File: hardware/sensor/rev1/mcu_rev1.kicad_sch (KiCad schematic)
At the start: 21 parts, among them IC1 STM8L051F3P6, J1 22-28-4044, J2 M20-9770342

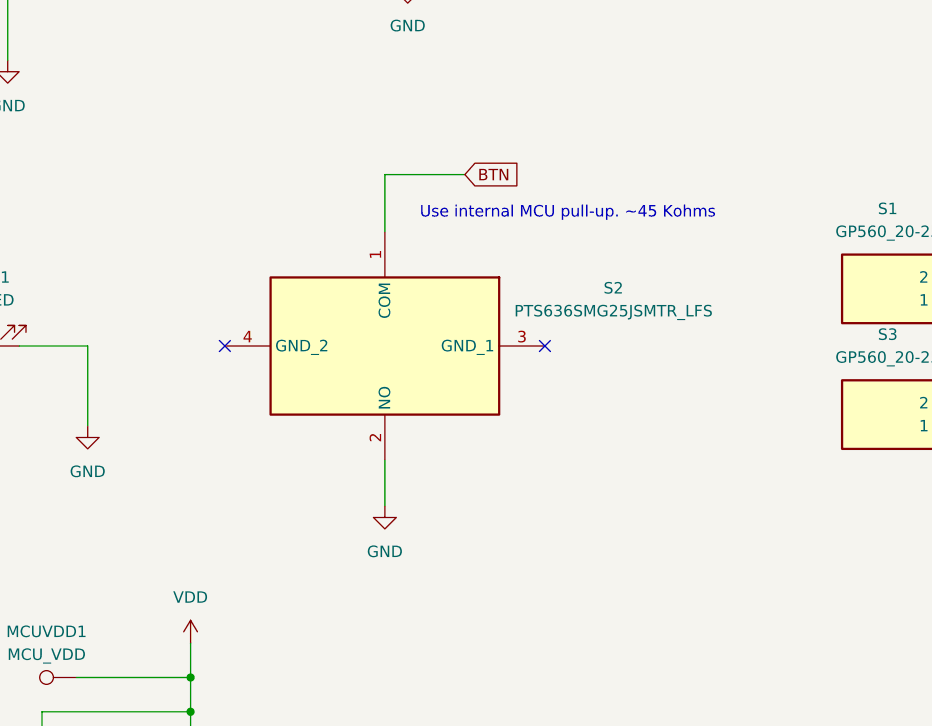
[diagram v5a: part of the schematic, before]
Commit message: EG-70 Adaptions according with JLCPCB production constraints.
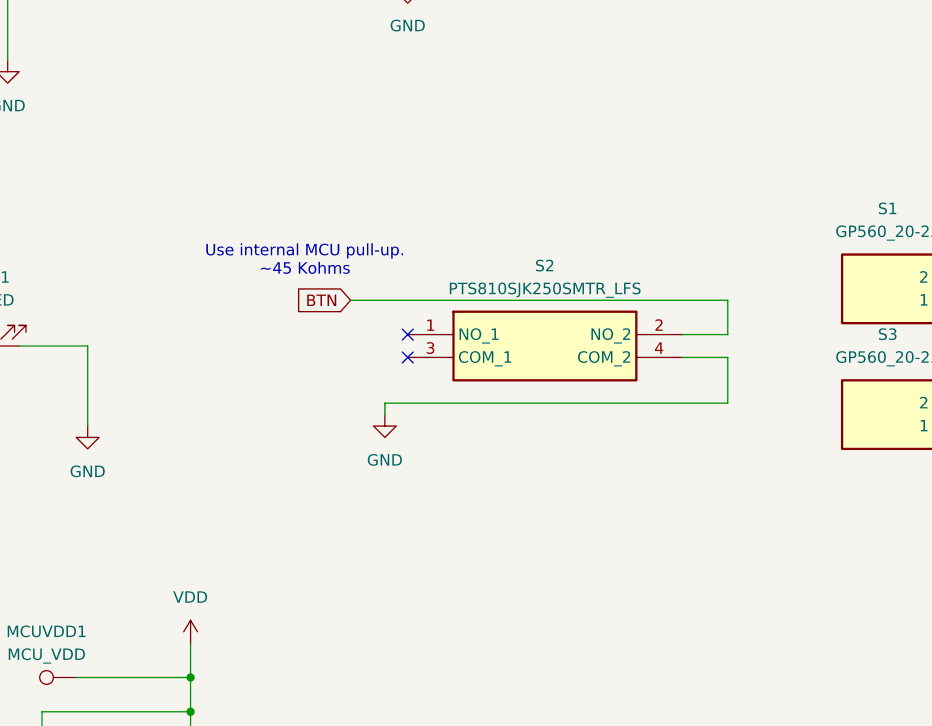
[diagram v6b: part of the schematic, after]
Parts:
- removed S2: PTS636SMG25JSMTR_LFS, MyParts:PTS636SMG25JSMTRLFS, symbol PTS636SMG25JSMTR_LFS:PTS636SMG25JSMTR_LFS
- added S2: PTS810SJK250SMTR_LFS, MyParts:PTS810SJK250SMTRLFS, symbol PTS810SJK250SMTR_LFS:PTS810SJK250SMTR_LFS
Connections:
- net BTN: now also S2.2 (NO_2)
- net GND: now also S2.4 (COM_2)
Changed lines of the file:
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@@
 		(company "NPX4U")
 	)
-	(text "Use internal MCU pull-up. ~45 Kohms"
+	(text "Use internal MCU pull-up.\n~45 Kohms"
 		(exclude_from_sim no)
-		(at 120.65 64.008 0)
+		(at 91.44 69.342 0)
 		(effects
 			(font
@@
 	)
 	(no_connect
-		(at 82.55 78.74)
+		(at 102.87 80.01)
 	)
 	(no_connect
-		(at 118.11 78.74)
+		(at 102.87 77.47)
 	)
 	(wire
@@
 	(wire
 		(pts
+			(xy 138.43 80.01) (xy 133.35 80.01)
+		)
+		(stroke
+			(width 0)
+			(type default)
+		)
+	)
+	(wire
+		(pts
 			(xy 133.35 168.91) (xy 133.35 166.37)
 		)
@@
 	(wire
 		(pts
+			(xy 133.35 77.47) (xy 138.43 77.47)
+		)
+		(stroke
+			(width 0)
+			(type default)
+		)
+	)
+	(wire
+		(pts
 			(xy 17.78 36.83) (xy 17.78 46.99)
 		)
@@
 	(wire
 		(pts
+			(xy 138.43 77.47) (xy 138.43 73.66)
+		)
+		(stroke
+			(width 0)
+			(type default)
+		)
+	)
+	(wire
+		(pts
+			(xy 100.33 85.09) (xy 138.43 85.09)
+		)
+		(stroke
+			(width 0)
+			(type default)
+		)
+	)
+	(wire
+		(pts
 			(xy 172.72 71.12) (xy 172.72 66.04)
 		)
@@
 	(wire
 		(pts
-			(xy 100.33 91.44) (xy 100.33 96.52)
-		)
-		(stroke
-			(width 0)
-			(type default)
-		)
-	)
-	(wire
-		(pts
 			(xy 60.96 148.59) (xy 83.82 148.59)
 		)
@@
 	(wire
 		(pts
-			(xy 100.33 59.69) (xy 100.33 66.04)
+			(xy 138.43 85.09) (xy 138.43 80.01)
 		)
 		(stroke
@@
 	(wire
 		(pts
-			(xy 100.33 59.69) (xy 109.22 59.69)
+			(xy 96.52 73.66) (xy 138.43 73.66)
 		)
 		(stroke
@@
 	(wire
 		(pts
+			(xy 100.33 86.36) (xy 100.33 85.09)
+		)
+		(stroke
+			(width 0)
+			(type default)
+		)
+	)
+	(wire
+		(pts
 			(xy 102.87 26.67) (xy 102.87 22.86)
 		)
@@
 	(global_label "BTN"
 		(shape input)
-		(at 109.22 59.69 0)
+		(at 96.52 73.66 180)
 		(fields_autoplaced yes)
 		(effects
@@
 				(size 1.27 1.27)
 			)
-			(justify left)
+			(justify right)
 		)
 		(property "Intersheetrefs" "${INTERSHEET_REFS}"
-			(at 115.7733 59.69 0)
+			(at 89.9667 73.66 0)
 			(effects
 				(font
 					(size 1.27 1.27)
 				)
-				(justify left)
+				(justify right)
 				(hide yes)
 			)
@@
 	(symbol
 		(lib_id "power:GND")
-		(at 100.33 96.52 0)
+		(at 100.33 86.36 0)
 		(unit 1)
 		(exclude_from_sim no)
@@
 		(dnp no)
 		(property "Reference" "#PWR022"
-			(at 100.33 102.87 0)
+			(at 100.33 92.71 0)
 			(effects
 				(font
@@
 		)
 		(property "Value" "GND"
-			(at 100.33 101.6 0)
+			(at 100.33 91.44 0)
 			(effects
 				(font
@@
 		)
 		(property "Footprint" ""
-			(at 100.33 96.52 0)
+			(at 100.33 86.36 0)
 			(effects
 				(font
@@
 		)
 		(property "Datasheet" ""
-			(at 100.33 96.52 0)
+			(at 100.33 86.36 0)
 			(effects
 				(font
@@
 		)
 		(property "Description" "Power symbol creates a global label with name \"GND\" , ground"
-			(at 100.33 96.52 0)
+			(at 100.33 86.36 0)
 			(effects
 				(font
@@
 	)
 	(symbol
-		(lib_id "PTS636SMG25JSMTR_LFS:PTS636SMG25JSMTR_LFS")
-		(at 100.33 66.04 270)
+		(lib_id "PTS810SJK250SMTR_LFS:PTS810SJK250SMTR_LFS")
+		(at 102.87 77.47 0)
 		(unit 1)
 		(exclude_from_sim no)
@@
 		(fields_autoplaced yes)
 		(property "Reference" "S2"
-			(at 125.73 72.3198 90)
+			(at 118.11 69.85 0)
 			(effects
 				(font
@@
 			)
 		)
-		(property "Value" "PTS636SMG25JSMTR_LFS"
-			(at 125.73 74.8598 90)
+		(property "Value" "PTS810SJK250SMTR_LFS"
+			(at 118.11 72.39 0)
 			(effects
 				(font
@@
 			)
 		)
-		(property "Footprint" "MyParts:PTS636SMG25JSMTRLFS"
-			(at 15.57 87.63 0)
+		(property "Footprint" "MyParts:PTS810SJK250SMTRLFS"
+			(at 129.54 172.39 0)
 			(effects
 				(font
@@
 			)
 		)
-		(property "Datasheet" "https://www.ckswitches.com/media/2779/pts636.pdf"
-			(at -84.43 87.63 0)
+		(property "Datasheet" "https://www.ckswitches.com/media/1476/pts810.pdf"
+			(at 129.54 272.39 0)
 			(effects
 				(font
@@
 			)
 		)
-		(property "Description" "Tactile Switches Tact 50mA 12VDC, 6.0x3.5, 2.5mm H, 180gf, J leads, Ground pin, White Actuator"
-			(at 100.33 66.04 0)
+		(property "Description" "TACTILE SWITCH, SPST, 0.05A, 16VDC, SMD"
+			(at 102.87 77.47 0)
 			(effects
 				(font
@@
 		)
 		(property "Height" "2.7"
-			(at -284.43 87.63 0)
+			(at 129.54 472.39 0)
 			(effects
 				(font
@@
 			)
 		)
-		(property "Mouser Part Number" "611-PTS636SMG25JSMTR"
-			(at -384.43 87.63 0)
+		(property "Mouser Part Number" "611-PTS810SJK250SMTR"
+			(at 129.54 572.39 0)
 			(effects
 				(font
@@
 			)
 		)
-		(property "Mouser Price/Stock" "https://www.mouser.co.uk/ProductDetail/CK/PTS636SMG25JSMTR-LFS?qs=jcD%2FCkGBYePRY%252BgAQy5esQ%3D%3D"
-			(at -484.43 87.63 0)
+		(property "Mouser Price/Stock" "https://www.mouser.co.uk/ProductDetail/CK/PTS810SJK250SMTR-LFS?qs=Imq1NPwxi77Ow0tzRIznfA%3D%3D"
+			(at 129.54 672.39 0)
 			(effects
 				(font
@@
 		)
 		(property "Manufacturer_Name" "LITTELFUSE"
-			(at -584.43 87.63 0)
+			(at 129.54 772.39 0)
 			(effects
 				(font
@@
 			)
 		)
-		(property "Manufacturer_Part_Number" "PTS636SMG25JSMTR LFS"
-			(at -684.43 87.63 0)
+		(property "Manufacturer_Part_Number" "PTS810SJK250SMTR LFS"
+			(at 129.54 872.39 0)
 			(effects
 				(font
@@
 			)
 		)
-		(property "Manufacturer" ""
-			(at 100.33 66.04 90)
-			(effects
-				(font
-					(size 1.27 1.27)
-				)
-				(hide yes)
-			)
-		)
-		(property "Supplier Link" ""
-			(at 100.33 66.04 90)
-			(effects
-				(font
-					(size 1.27 1.27)
-				)
-				(hide yes)
-			)
+		(pin "3"
 		)
-		(pin "4"
+		(pin "2"
 		)
 		(pin "1"
 		)
-		(pin "3"
-		)
-		(pin "2"
+		(pin "4"
 		)
 		(instances
 			(project ""
-				(path "/c9ab58dc-163d-4c4e-8d12-3a07665777cf"
-					(reference "S3")
-					(unit 1)
-				)
-			)
-			(project "sensor_rev1"
 				(path "/d3cb7130-decc-418b-958e-e5d84a8d867f/ec220677-d66d-4ee1-961f-1c93fb46783a"
 					(reference "S2")

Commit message: EG-70 XTAL replaced according with JLCPCB constraints and capacitors adjusted accordingly.
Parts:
- D1: Manufacturer_Part_Number 597-3008-207F -> 5973008207F
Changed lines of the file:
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@@
 			)
 		)
-		(property "Manufacturer_Part_Number" "597-3008-207F "
+		(property "Manufacturer_Part_Number" "5973008207F "
 			(at 55.88 78.74 0)
 			(effects
